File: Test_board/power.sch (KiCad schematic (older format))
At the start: 9 parts

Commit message: Wired the whole first sheet
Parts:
- added Q?: Q_PMOS_DGS, symbol Q_PMOS_DGS
- gave numbers to parts that had none: 9
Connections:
- net at J12.1: now also Q?.1 (D); no longer J14.1 (VBUS)
- net GND: now reaches J13.1, J14.5 (GND), J14.6 (Shield)
- net GND: now also Q?.2 (G)
- net at U5.10 (PGND): now also U5.11 (PGND), U5.21 (PGND), U5.8 (BURST)
- net at U5.15 (L1): now also U5.16 (L1), U5.17 (L1)
- net at U5.18 (L2): now also U5.19 (L2)
- net at U5.2 (VOUT): now also U5.3 (VOUT)
- net VIN: now reaches U5.4 (VIN)
- net VIN: now also J14.1 (VBUS), U5.5 (VIN), U5.6 (VIN), Q?.3 (S)
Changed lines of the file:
@@
 $EndDescr
 $Comp
-L 4.19mmBananaJack J?
+L 4.19mmBananaJack J10
 U 1 1 59FAC5A6
 P 950 750
-F 0 "J?" H 950 600 60  0000 C CNN
+F 0 "J10" H 950 600 60  0000 C CNN
 F 1 "4.19mmBananaJack" H 950 900 60  0000 C CNN
 F 2 "" H 950 750 60  0001 C CNN
@@
 $EndComp
 $Comp
-L 4.19mmBananaJack J?
+L 4.19mmBananaJack J11
 U 1 1 59FAC5D9
 P 950 1150
-F 0 "J?" H 950 1000 60  0000 C CNN
+F 0 "J11" H 950 1000 60  0000 C CNN
 F 1 "4.19mmBananaJack" H 950 1300 60  0000 C CNN
 F 2 "" H 950 1150 60  0001 C CNN
@@
 MPPT input
 $Comp
-L 4.19mmBananaJack J?
+L 4.19mmBananaJack J12
 U 1 1 59FAC601
 P 950 4450
-F 0 "J?" H 950 4300 60  0000 C CNN
+F 0 "J12" H 950 4300 60  0000 C CNN
 F 1 "4.19mmBananaJack" H 950 4600 60  0000 C CNN
 F 2 "" H 950 4450 60  0001 C CNN
@@
 $EndComp
 $Comp
-L 4.19mmBananaJack J?
+L 4.19mmBananaJack J13
 U 1 1 59FAC66E
 P 950 6000
-F 0 "J?" H 950 5850 60  0000 C CNN
-F 1 "4.19mmBananaJack" H 950 6150 60  0000 C CNN
+F 0 "J13" H 950 5850 60  0000 C CNN
+F 1 "4.19mmBananaJack" V 750 6000 60  0000 C CNN
 F 2 "" H 950 6000 60  0001 C CNN
 F 3 "" H 950 6000 60  0001 C CNN
@@
 $EndComp
 $Comp
-L USB_OTG J?
+L USB_OTG J14
 U 1 1 59FAC68F
 P 1000 5200
-F 0 "J?" H 800 5650 50  0000 L CNN
+F 0 "J14" H 800 5650 50  0000 L CNN
 F 1 "USB_OTG" H 800 5550 50  0000 L CNN
 F 2 "" H 1150 5150 50  0001 C CNN
@@
 $EndComp
 Wire Wire Line
-	900  5600 1200 5600
+	900  5600 1000 5600
 Wire Wire Line
-	1300 5000 1300 4450
+	1000 5600 1200 5600
 Wire Wire Line
-	1300 4450 1200 4450
+	1200 4450 1350 4450
 Wire Wire Line
 	1200 5600 1200 6000
@@
 Converter input
 $Comp
-L LT3652 U?
+L LT3652 U3
 U 1 1 59FACBE2
 P 2950 1350
-F 0 "U?" H 3200 950 60  0000 C CNN
+F 0 "U3" H 3200 950 60  0000 C CNN
 F 1 "LT3652" H 2950 1750 60  0000 C CNN
 F 2 "" H 2950 1350 60  0001 C CNN
@@
 $EndComp
 $Comp
-L LT3652 U?
+L LT3652 U4
 U 1 1 59FACC3B
 P 2950 2550
-F 0 "U?" H 3200 2150 60  0000 C CNN
+F 0 "U4" H 3200 2150 60  0000 C CNN
 F 1 "LT3652" H 2950 2950 60  0000 C CNN
 F 2 "" H 2950 2550 60  0001 C CNN
@@
 $EndComp
 $Comp
-L LTC3113 U?
+L LTC3113 U5
 U 1 1 59FACF9C
 P 3300 4950
-F 0 "U?" H 3500 4350 60  0000 C CNN
+F 0 "U5" H 3500 4350 60  0000 C CNN
 F 1 "LTC3113" H 3300 5550 60  0000 C CNN
 F 2 "" H 3250 4900 60  0001 C CNN
@@
 $EndComp
 $Comp
-L LTC3113 U?
+L LTC3113 U6
 U 1 1 59FAD00D
 P 3300 6900
-F 0 "U?" H 3500 6300 60  0000 C CNN
+F 0 "U6" H 3500 6300 60  0000 C CNN
 F 1 "LTC3113" H 3300 7500 60  0000 C CNN
 F 2 "" H 3250 6850 60  0001 C CNN
@@
 Text Notes 3250 6250 0    60   ~ 0
 5V
+$Comp
+L Q_PMOS_DGS Q?
+U 1 1 59FD2610
+P 1550 4550
+F 0 "Q?" H 1750 4600 50  0000 L CNN
+F 1 "Q_PMOS_DGS" H 1750 4500 50  0000 L CNN
+F 2 "" H 1750 4650 50  0001 C CNN
+F 3 "" H 1550 4550 50  0001 C CNN
+	1    1550 4550
+	0    -1   -1   0
+$EndComp
+Wire Wire Line
+	1300 5000 1800 5000
+Wire Wire Line
+	1800 5000 1800 4450
+Wire Wire Line
+	1800 4450 1750 4450
+$Comp
+L GND #PWR?
+U 1 1 59FD2668
+P 1550 4800
+F 0 "#PWR?" H 1550 4550 50  0001 C CNN
+F 1 "GND" H 1550 4650 50  0000 C CNN
+F 2 "" H 1550 4800 50  0001 C CNN
+F 3 "" H 1550 4800 50  0001 C CNN
+	1    1550 4800
+	1    0    0    -1
+$EndComp
+Wire Wire Line
+	1550 4800 1550 4750
+Wire Wire Line
+	2700 5200 2700 5400
+Wire Wire Line
+	2700 5400 2700 5700
+Wire Wire Line
+	2700 5700 3300 5700
+Wire Wire Line
+	3300 5700 3800 5700
+Wire Wire Line
+	3800 5700 3800 5400
+Connection ~ 3300 5700
+Wire Wire Line
+	2700 5400 2800 5400
+Wire Wire Line
+	2800 5200 2700 5200
+Connection ~ 2700 5400
+Wire Wire Line
+	2800 4800 2800 4900
+Wire Wire Line
+	2800 4900 2800 5000
+Connection ~ 2800 4900
+Wire Wire Line
+	2800 4600 2800 4700
+Wire Wire Line
+	3800 4600 3800 4700
+Wire Wire Line
+	3800 4800 3800 4900
+Wire Wire Line
+	3800 4900 3800 5000
+Connection ~ 3800 4900
+Text Label 1800 4450 0    60   ~ 0
+VIN
+Text Label 2800 4900 2    60   ~ 0
+VIN
+$Comp
+L GND #PWR?
+U 1 1 59FD2EC2
+P 1200 6000
+F 0 "#PWR?" H 1200 5750 50  0001 C CNN
+F 1 "GND" H 1200 5850 50  0000 C CNN
+F 2 "" H 1200 6000 50  0001 C CNN
+F 3 "" H 1200 6000 50  0001 C CNN
+	1    1200 6000
+	1    0    0    -1
+$EndComp
+Wire Wire Line
+	1200 6000 1200 6000
+Connection ~ 1200 6000
 $EndSCHEMATC

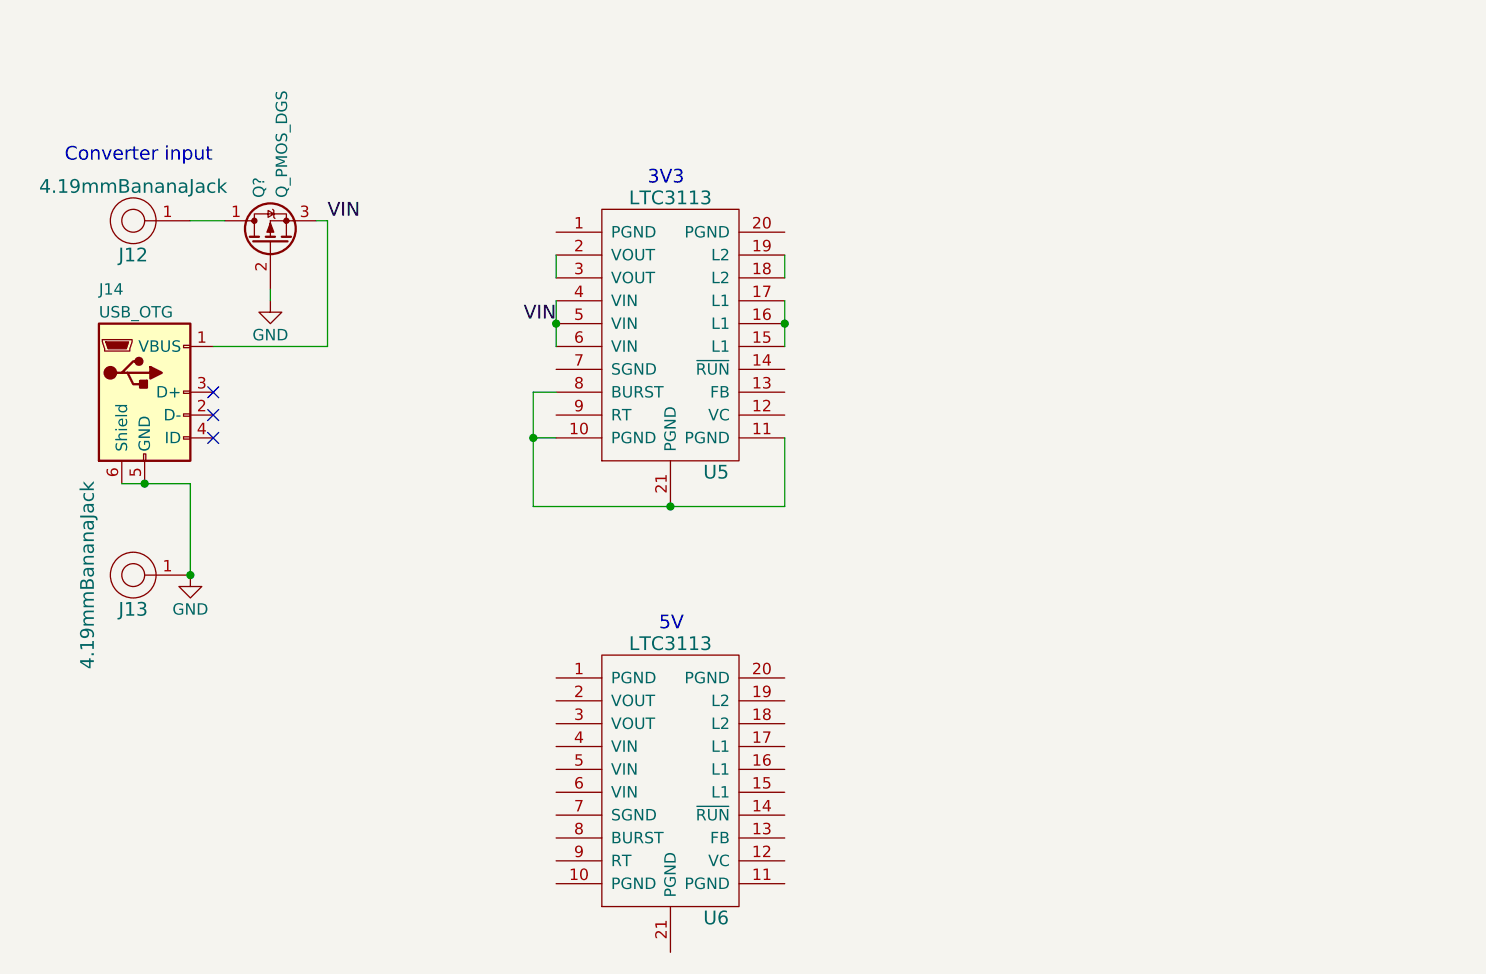
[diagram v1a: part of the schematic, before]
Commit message: Wired most of power converters, only VC pins to wire
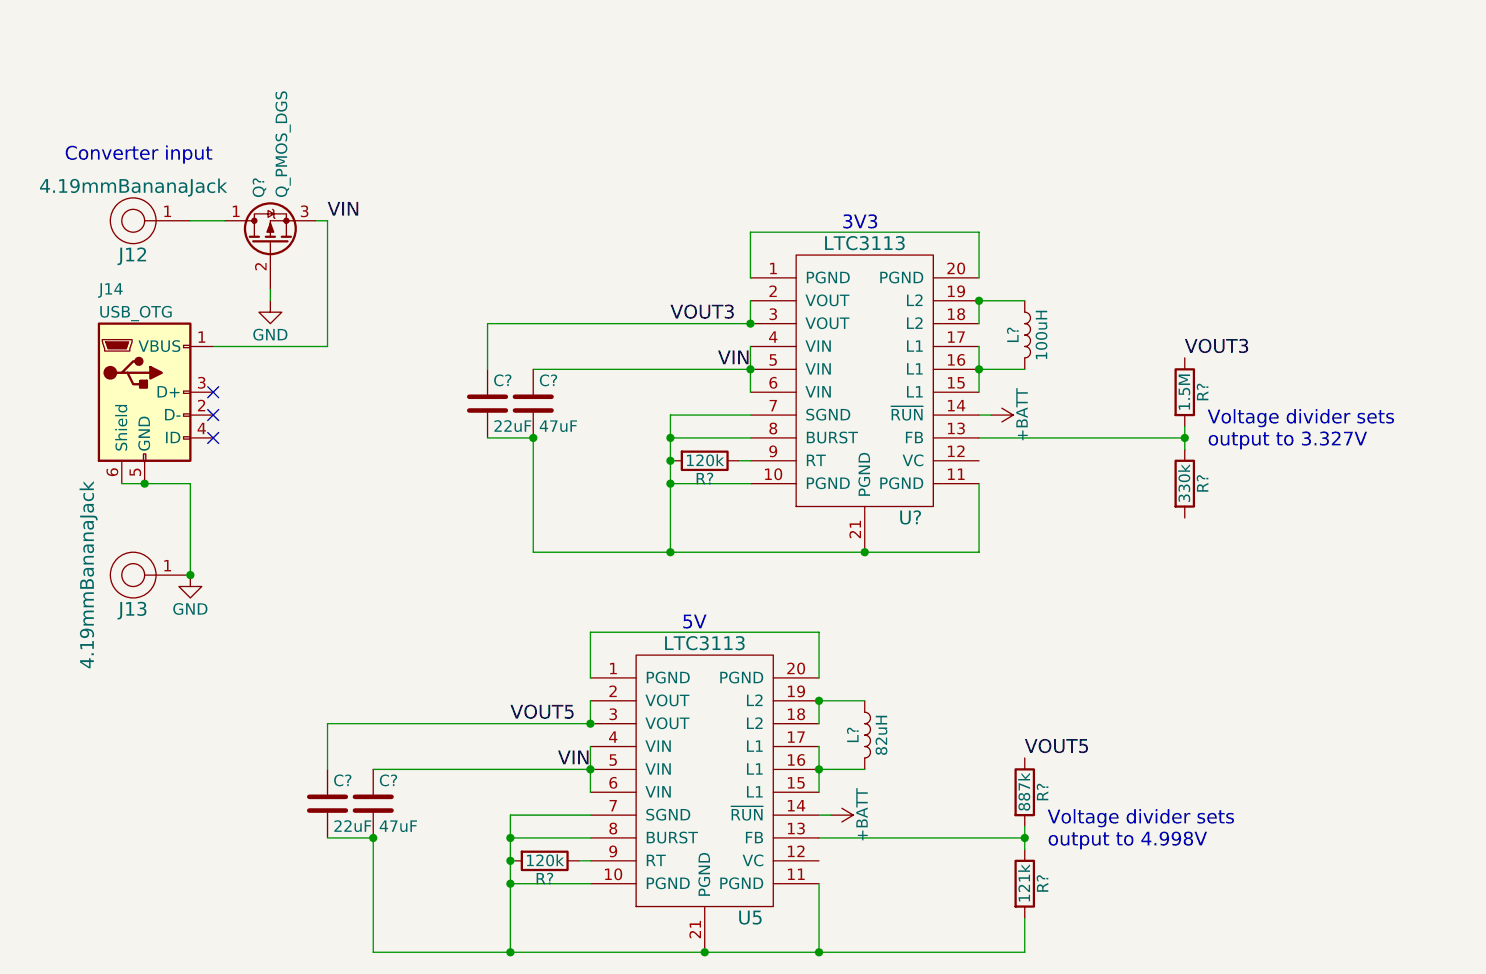
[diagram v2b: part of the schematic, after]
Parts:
- removed U6: LTC3113, symbol LTC3113
- added C? (x2): 22uF, symbol C
- added C? (x2): 47uF, symbol C
- added L?: 82uH, symbol L
- added L?: 100uH, symbol L
- added R? (x2): 120k, 0805, symbol R
- added R?: 887k, symbol R
- added R?: 121k, symbol R
- added R?: 1.5M, symbol R
- added R?: 330k, symbol R
- added U?: LTC3113, symbol LTC3113
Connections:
- net VIN: now also C?.1, C?.1, U?.4 (VIN), U?.5 (VIN), U?.6 (VIN)
- net at U5.1 (PGND): now also U5.20 (PGND)
- net at U5.10 (PGND), U5.11 (PGND), U5.21 (PGND)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: now also U5.7 (SGND), C?.2, C?.2, R?.2, R?.2
- net at U5.13 (FB): now also R?.1, R?.2
- net +BATT: now reaches U5.14 (~RUN)
- net +BATT: now also U?.14 (~RUN)
- net at U5.15 (L1), U5.16 (L1), U5.17 (L1): now also L?.2
- net at U5.18 (L2), U5.19 (L2): now also L?.1
- net VOUT5: now reaches U5.2 (VOUT), U5.3 (VOUT)
- net VOUT5: now also C?.1, R?.1
- net at U5.9 (RT): now also R?.1
- new net: U?.1 (PGND), U?.20 (PGND)
- new net: C?.2, C?.2, R?.2, U?.10 (PGND), U?.11 (PGND), U?.21 (PGND), U?.7 (SGND), U?.8 (BURST)
- new net: R?.1, R?.2, U?.13 (FB)
- new net: L?.2, U?.15 (L1), U?.16 (L1), U?.17 (L1)
- new net: L?.1, U?.18 (L2), U?.19 (L2)
- new net: R?.1, U?.9 (RT)
- new net VOUT3: C?.1, R?.1, U?.2 (VOUT), U?.3 (VOUT)
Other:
- note added: "Voltage divider sets\noutput to 3.327V"
- note added: "Voltage divider sets\noutput to 4.998V"
- moved on the sheet: U5

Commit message: Finished schematic
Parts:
- removed Q?: Q_PMOS_DGS, symbol Q_PMOS_DGS
- removed R?: 887k, symbol R
- removed R?: 121k, symbol R
- removed U4: LT3652, symbol LT3652
- added C14, C15, C16, C17, C20, C21: 0.1uF, Capacitors_SMD:C_0805_HandSoldering, symbol C
- added C18, C19: 1uF, symbol C
- added C22, C23: 10uF, symbol C
- added C24, C25: 100uF, symbol C
- added C26, C27: 12pF, symbol C
- added C28, C29: 680pF, symbol C
- added C30, C31: 47pF, symbol C
- added D1, D2: MBRS140, symbol D_Schottky
- added D3, D4: MBRS340, symbol D_Schottky
- added D5, D6: D, symbol D
- added J15, J16: TEST_1P, Measurement_Points:Measurement_Point_Round-SMD-Pad_Big, symbol TEST_1P
- added L3, L4: 6.8uH, symbol L
- added R10, R9: 20m, symbol R
- added R13, R14, R15, R16, R17, R18: 100k, symbol R
- added R19, R20: 179k, symbol R
- added R21, R22: 330k, symbol R
- added R23, R24, R25, R26: 180k, symbol R
- added R27, R28: 50m, symbol R
- added R29, R30: 49.9k, symbol R
- added R31: 887k, symbol R
- added R32: 121k, symbol R
- added R33, R34: 6.49k, symbol R
- added U10, U11, U4, U9: INA219, symbol INA219
- added U8: LT3652, symbol LT3652
- C10, C12: renamed from C?; value 22uF -> 100uF
- L1: renamed from L?; value 82uH -> 2.2uH
- L2: renamed from L?; value 100uH -> 2.2uH
- R11: renamed from R?; value 1.5M -> 825k
- R12: renamed from R?; value 330k -> 182k
- R7, R8: renamed from R?; value 120k -> 90.9k; footprint 0805 -> (none)
- gave numbers to parts that had none: 3
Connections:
- net +BATT: now also C11.1, C13.1, U5.4 (VIN), U5.5 (VIN), U5.6 (VIN), U7.4 (VIN), U7.5 (VIN), U7.6 (VIN), R9.2, U10.7 (IN-), U9.7 (IN-)
- net GND: now also C10.2, C11.2, C12.2, C13.2, J11.1, R12.2, R7.2, R8.2, U3.13 (GND), U3.6 (TIMER), U5.1 (PGND), U5.10 (PGND), U5.11 (PGND), U5.20 (PGND), U5.21 (PGND), U5.7 (SGND), U5.8 (BURST), U7.1 (PGND), U7.10 (PGND), U7.11 (PGND), U7.20 (PGND), U7.21 (PGND), U7.7 (SGND), U7.8 (BURST), C14.1, C15.1, C16.2, C17.2, C20.1, C21.1, C22.2, C23.2, C24.2, C25.2, D3.2 (A), D4.2 (A), R15.2, R18.2, R21.2, R22.2, R32.2, U10.1 (A1), U10.6 (GND), U11.1 (A1), U11.6 (GND), U4.1 (A1), U4.2 (A0), U4.6 (GND), U8.13 (GND), U8.6 (TIMER), U9.1 (A1), U9.2 (A0), U9.6 (GND)
- net VOUT3: now also J16.1, R10.1, R33.1, U11.8 (IN+), U4.8 (IN+)
- net VOUT5: now also J15.1
- net MPPT_IN: now reaches J10.1
- net MPPT_IN: now also D1.2 (A), D2.2 (A)
- net VINPUT: now reaches J12.1
- net VINPUT: now also J14.1 (VBUS)
- net at U3.1 (Vin): now also U3.3 (~SHDN), C16.1, D1.1 (K), R13.1
- net at U3.10 (SENSE): now also L3.1, R27.2
- net at U3.11 (BOOST): now also C18.2, D5.1 (K)
- net at U3.12 (SW): now also C18.1, D3.1 (K), L3.2
- net at U3.2 (Vin_reg): now also R14.2, R15.1
- net at U3.7 (Vfb): now also R19.2
- net MPPT_OUT: now reaches U3.9 (BAT)
- net MPPT_OUT: now also C22.1, C23.1, C24.1, C25.1, D5.2 (A), D6.2 (A), R23.1, R24.1, R25.1, R26.1, R27.1, R28.1, R9.1, U10.8 (IN+), U8.9 (BAT), U9.8 (IN+)
- net at U5.12 (VC): now also C27.2, R30.2
- net at U5.13 (FB): now also C27.1, C29.1, C31.2, R31.2, R32.1
- net at U7.12 (VC): now also C26.2, R29.2
- net at R11.2, R12.1, U7.13 (FB): now also C26.1, C28.1, C30.2
- removed net VIN: C11.1, C13.1, J14.1 (VBUS), U5.4 (VIN), U5.5 (VIN), U5.6 (VIN), U7.4 (VIN), U7.5 (VIN), U7.6 (VIN)
- new net: C28.2, R29.1
- new net: C30.1, R33.2
- new net: C29.2, R30.1
- new net: C31.1, R34.2
- new net: R13.2, R14.1
- new net: R19.1, R21.1, R23.2, R24.2
- new net: C17.1, D2.1 (K), R16.1, U8.1 (Vin), U8.3 (~SHDN)
- new net: L4.1, R28.2, U8.10 (SENSE)
- new net: C19.2, D6.1 (K), U8.11 (BOOST)
- new net: C19.1, D4.1 (K), L4.2, U8.12 (SW)
- new net: R17.2, R18.1, U8.2 (Vin_reg)
- new net: R20.2, U8.7 (Vfb)
- new net: R16.2, R17.1
- new net: R20.1, R22.1, R25.2, R26.2
- new net +3V3: C14.2, C15.2, C20.2, C21.2, R10.2, U10.2 (A0), U10.5 (VCC), U11.2 (A0), U11.5 (VCC), U11.7 (IN-), U4.5 (VCC), U4.7 (IN-), U9.5 (VCC)
- new net +5V: R31.1, R34.1
- new net SCL: U10.4 (SCL), U11.4 (SCL), U4.4 (SCL), U9.4 (SCL)
- new net SDA: U10.3 (SDA), U11.3 (SDA), U4.3 (SDA), U9.3 (SDA)
- no-connect marks 3 -> 9
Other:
- note added: "2X MPPT"
- note added: "3V3 bus monitoring"
- note added: "Input"
- note added: "RAW bus monitoring"
- note added: "RAW-to-bus voltage conversion"
- note removed: "Converter input"
- note removed: "MPPT input"
- note removed: "Voltage divider sets\noutput to 3.327V"
- note removed: "Voltage divider sets\noutput to 4.998V"
- moved on the sheet: C10, C11, C12, C13, J11, J12, J13, J14, L1, L2, R11, R12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

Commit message: Updated libraries, footprint assignments, and created protector for barometer
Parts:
- C10, C11, C12, C13, C18, C19, C22, C23, C24, C25, C26, C27, C28, C29, C30, C31: footprint (none) -> Capacitors_SMD:C_0805_HandSoldering
- D1, D2: footprint (none) -> Diodes_SMD:D_SMB
- D3, D4: footprint (none) -> Diodes_SMD:D_SMC
- J10, J11, J12, J13: footprint (none) -> aleksandr_footprints:4.19Banana
- L1, L2: footprint (none) -> aleksandr_footprints:L-7443330220
- L3, L4: footprint (none) -> aleksandr_footprints:L-SLF6028T-6R8M1R5-PF
- R10, R27, R28, R9: footprint (none) -> Resistors_SMD:R_1206_HandSoldering
- R11, R12, R13, R14, R15, R16, R17, R18, R19, R20, R21, R22, R23, R24, R25, R26, R29, R30, R31, R32, R33, R34, R7, R8: footprint (none) -> Resistors_SMD:R_0805_HandSoldering
- U10, U11, U4, U9: footprint (none) -> Housings_SOIC:SOIC-8_3.9x4.9mm_Pitch1.27mm
- U3, U8: footprint (none) -> aleksandr_footprints:12MSOP-E
- U5, U7: footprint (none) -> aleksandr_footprints:20TSSOP-E
